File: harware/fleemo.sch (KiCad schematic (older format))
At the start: 44 parts, among them P1 CONN_01X02, P2 CONN_01X03, P3 RESET_PAD, Q1 STD2HNK60Z-1, U1 AMS1117, U2 wurth-750312723, U3 UCC28700, U4 STM32F030F4Px, Y1 8Mhz

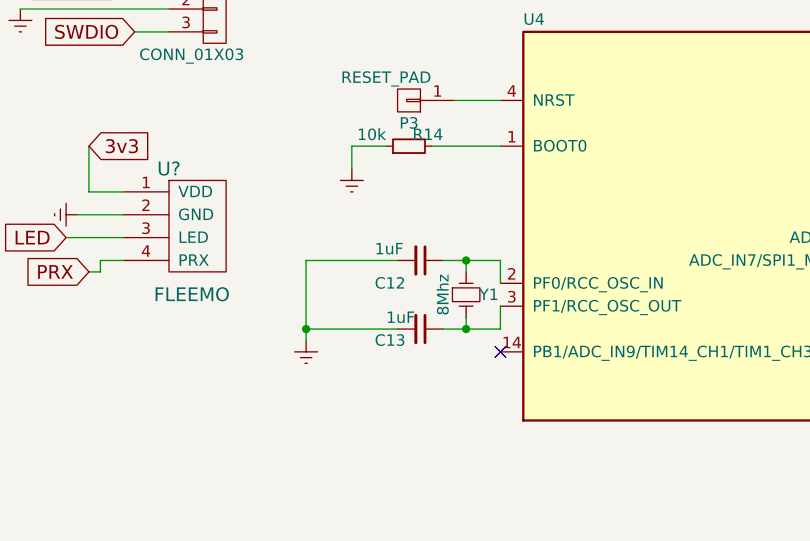
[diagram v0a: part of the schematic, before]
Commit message: change bypass cap value
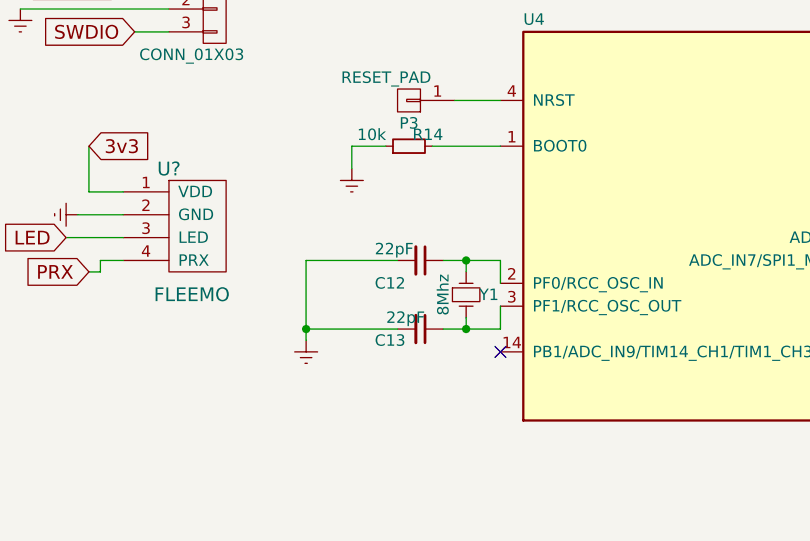
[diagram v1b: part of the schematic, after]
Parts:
- C12, C13: value 1uF -> 22pF
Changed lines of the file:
@@
 P 6450 5200
 F 0 "C12" V 6550 5000 50  0000 L CNN
-F 1 "1uF" V 6400 5000 50  0000 L CNN
+F 1 "22pF" V 6400 5000 50  0000 L CNN
 F 2 "" H 6450 5200 50  0000 C CNN
 F 3 "" H 6450 5200 50  0000 C CNN
@@
 P 6450 5500
 F 0 "C13" V 6500 5300 50  0000 L CNN
-F 1 "1uF" V 6400 5350 50  0000 L CNN
+F 1 "22pF" V 6400 5350 50  0000 L CNN
 F 2 "" H 6450 5500 50  0000 C CNN
 F 3 "" H 6450 5500 50  0000 C CNN
